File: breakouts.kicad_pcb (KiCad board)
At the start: 2 copper layers, 100 x 92.6 mm, 211 parts, among them IC901 ATTINY85-S, J1101 USB_MINI-B, J1201 JACK_5P, J201 USB_MINI-B, J301 USB_MINI-B, J401 SMA, J801 USB_MINI-B, K1201 CONN_3, K1301 CONN_3, K601 CONN_3, K801 CONN_3, P1001 CONN_4, P1002 CONN_4, P1101 CONN_6, P1102 CONN_6, P1201 CONN_2, P1202 CONN_2, P1203 CONN_2, P1301 CONN_2, P201 CONN_2, P202 CONN_2, P203 CONN_2, P301 CONN_6, P302 CONN_6, P401 CONN_8, P402 CONN_8, P501 CONN_2, P502 CONN_2, P701 POWER, P702 PORT B, P703 PORT C, P704 PORT D, P705 ISP, P801 PORT B, P802 PORT C, P803 PORT D, P804 ISP, P901 CONN_8, P902 ISP, SW701 SW_PUSH, SW801 SW_PUSH, SW901 SW_PUSH, U1001 SST25VF016B, U1101 FT230X-QFN, U1201 TDA1517ATW, U1301 MCP7940M, U301 FT230X, U401 MRF49XA, U501 SP6641A/B, U601 NX1117C33Z, U701 ATMEGA88PA-A, U801 ATMEGA32U2, X1301 32.768kHz, X401 10MHz, X701 12MHz 18pF, X801 16MHz 18pF

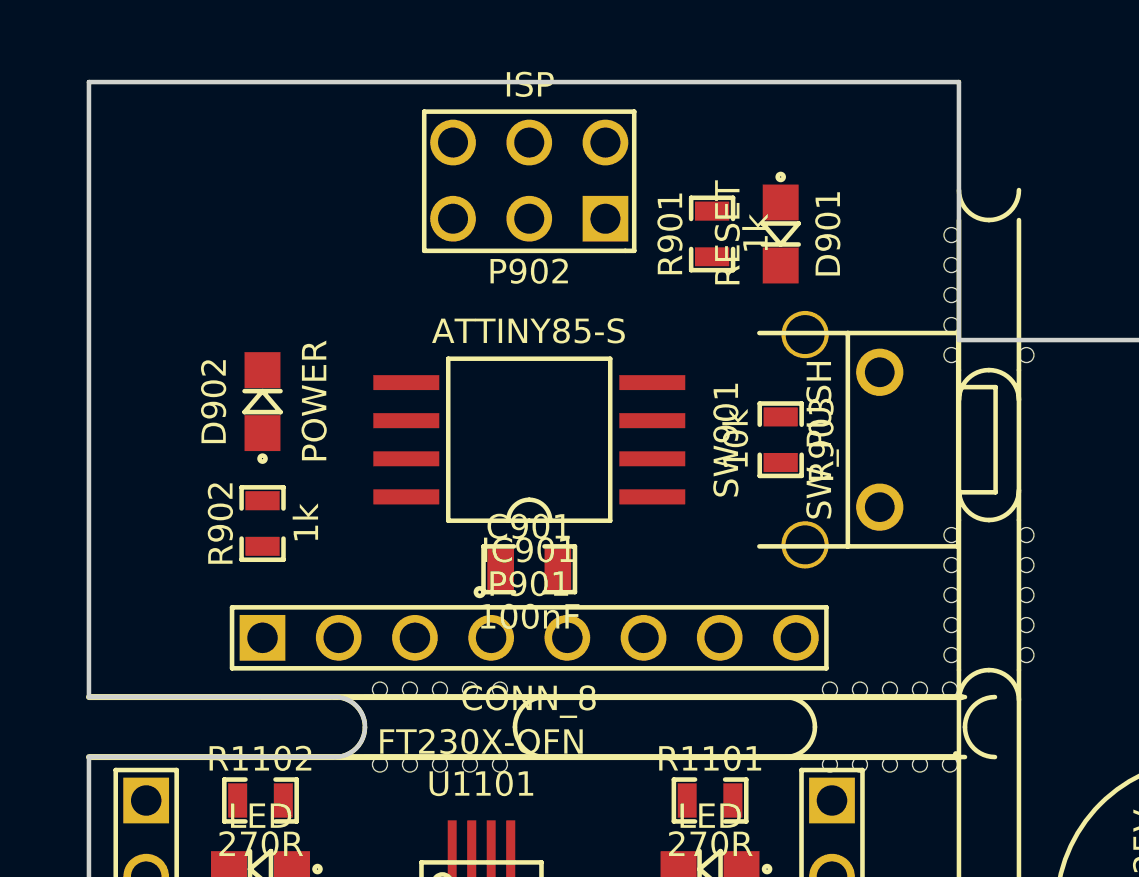
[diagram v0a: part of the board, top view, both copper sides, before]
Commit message: Route AVR ATtinyx5 board
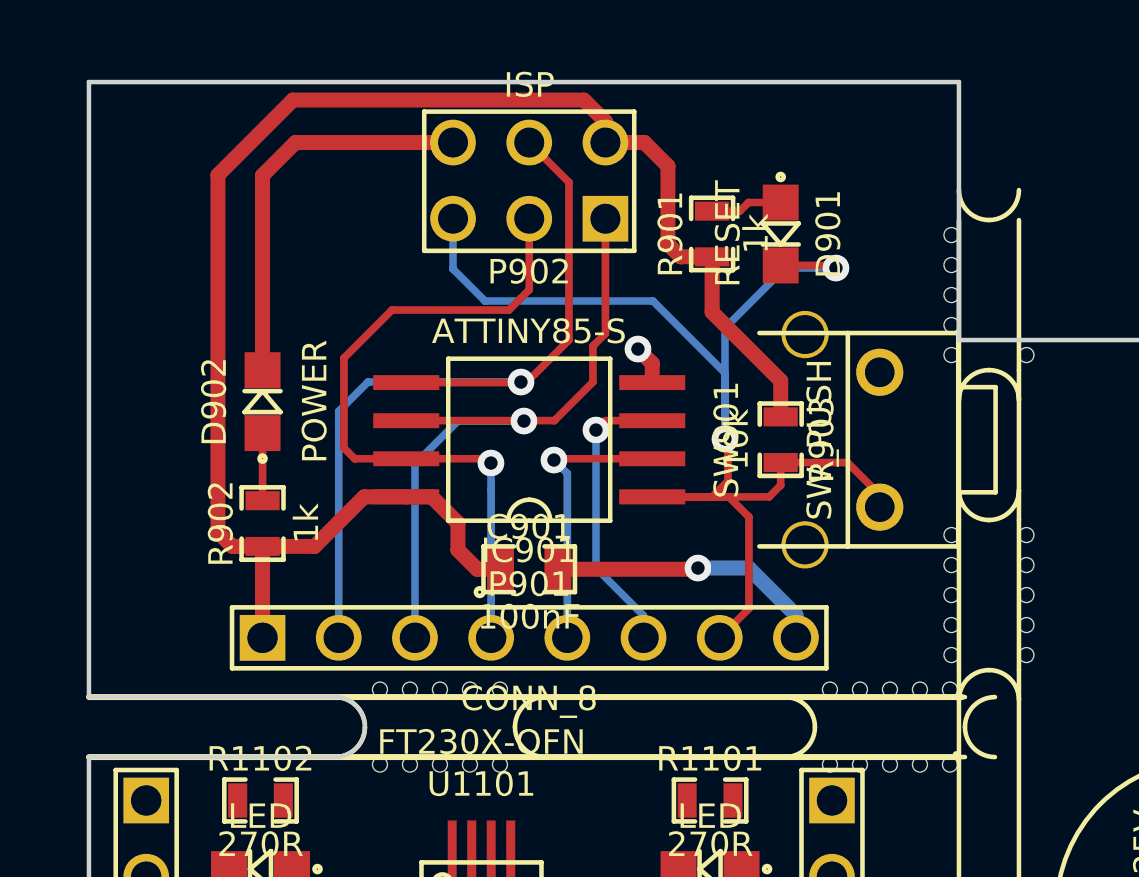
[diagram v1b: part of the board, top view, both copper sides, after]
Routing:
- net VCC8: track 0.00 -> 54.7 mm
- net /AVR-ATtinyx5/PB5: track 0.00 -> 44.0 mm, vias 0 -> 2
- net /AVR-ATtinyx5/MOSI: track 0.00 -> 27.2 mm, vias 0 -> 1
- net GND8: track 0.00 -> 24.0 mm, vias 0 -> 2
- net /AVR-ATtinyx5/PB2: track 0.00 -> 23.4 mm, vias 0 -> 1
- net /AVR-ATtinyx5/MISO: track 0.00 -> 22.4 mm, vias 0 -> 1
- net /AVR-ATtinyx5/PB4: track 0.00 -> 9.59 mm, vias 0 -> 1
- net /AVR-ATtinyx5/PB3: track 0.00 -> 9.40 mm, vias 0 -> 1
- net N-00000124: track 0.00 -> 2.40 mm
- net N-00000123: track 0.00 -> 2.25 mm
- added copper zone on B.Cu, net GND8

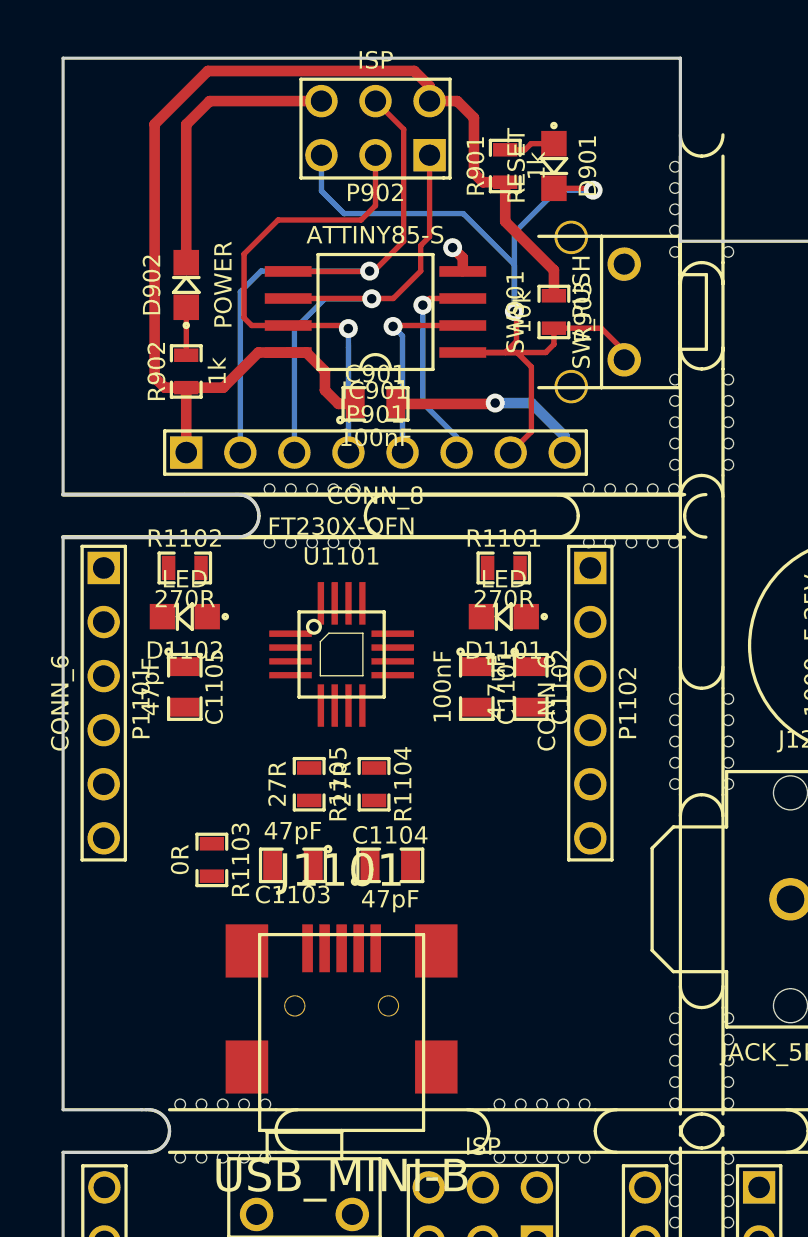
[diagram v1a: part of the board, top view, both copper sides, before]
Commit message: Rework and route FT230X-QFN board
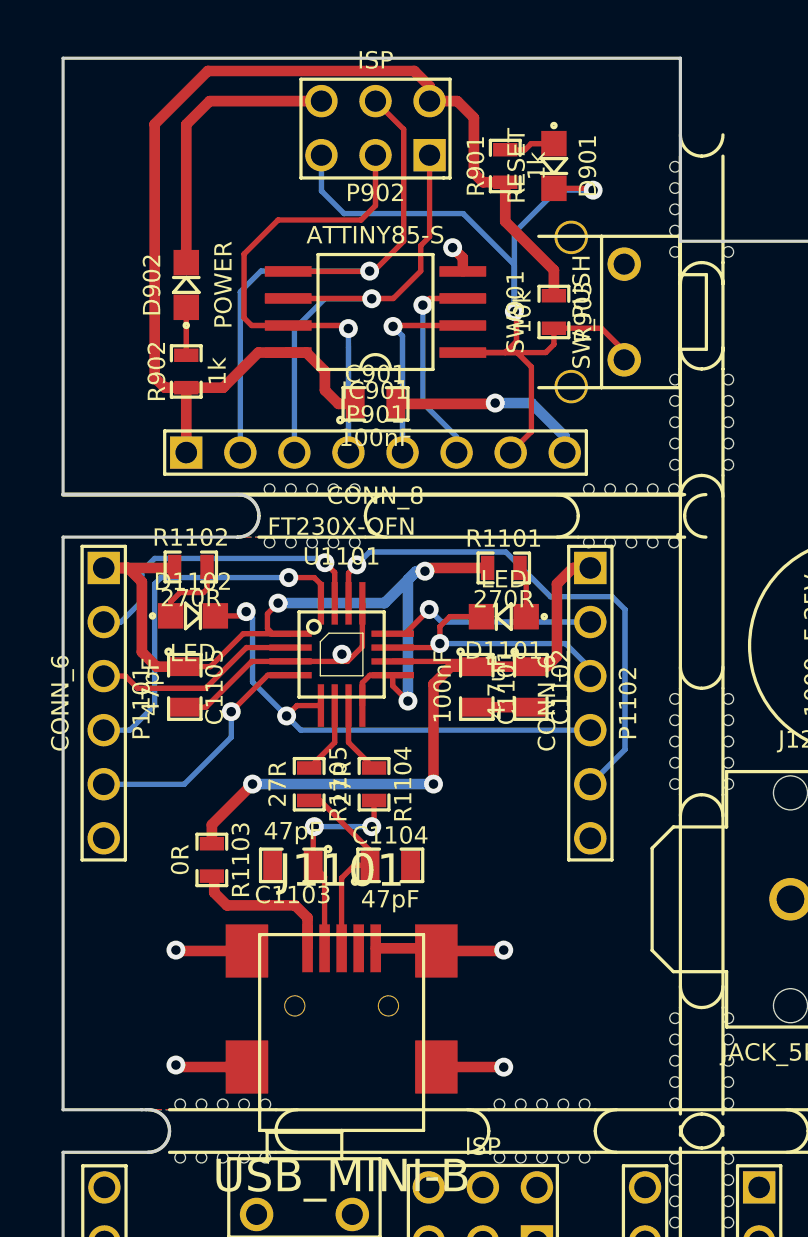
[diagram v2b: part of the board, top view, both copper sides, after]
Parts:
- moved D1102 0.38 mm to (32.1, 81.1), turned to 0 degrees
- moved R1102 0.29 mm to (32.0, 78.8)
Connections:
- J1101 pad 4: N-00000154 -> (no net)
- J1201 pad 3: N-00000177 -> (no net)
- J1201 pad 4: N-00000178 -> (no net)
- J201 pad 4: N-000007 (its old number) -> (no net)
- J301 pad 4: N-0000025 -> (no net)
- J801 pad 4: N-0000092 (its old number) -> (no net)
- P1101 pad 1: VCC3 -> /FT230X-QFN/VCCIO
- P1102 pad 1: /FT230X-QFN/VCCIO -> VCC3
- U1201 pad 1: N-00000170 (its old number) -> (no net)
- U1201 pad 14: N-00000176 -> (no net)
- U1201 pad 19: N-00000166 (its old number) -> (no net)
- U1201 pad 2: N-00000171 -> (no net)
- U1201 pad 20: N-00000175 -> (no net)
- U1201 pad 6: N-00000172 -> (no net)
- U1201 pad 7: N-00000173 -> (no net)
- U1301 pad 3: N-00000183 (its old number) -> (no net)
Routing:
- net /FT230X-QFN/VCCIO: track 0.00 -> 40.2 mm, vias 0 -> 3
- net VCC3: track 0.00 -> 32.5 mm, vias 0 -> 2
- net GND3: track 0.00 -> 30.2 mm, vias 0 -> 5
- net /FT230X-QFN/CBUS3: track 0.00 -> 24.8 mm, vias 0 -> 1
- net /FT230X-QFN/CBUS2: track 0.00 -> 23.6 mm, vias 0 -> 2
- net /FT230X-QFN/~RTS: track 0.00 -> 17.5 mm, vias 0 -> 1
- net /FT230X-QFN/TxD: track 0.00 -> 14.6 mm, vias 0 -> 1
- net /FT230X-QFN/CBUS1: track 0.00 -> 13.2 mm, vias 0 -> 1
- net /FT230X-QFN/~CTS: track 0.00 -> 11.6 mm, vias 0 -> 1
- net /FT230X-QFN/CBUS0: track 0.00 -> 10.00 mm, vias 0 -> 1
- net N-00000151: track 0.00 -> 9.93 mm, vias 0 -> 2
- net /FT230X-QFN/RxD: track 0.00 -> 9.81 mm
- net N-00000152: track 0.00 -> 9.41 mm
- net N-00000150: track 0.00 -> 7.13 mm
- net N-00000156: track 0.00 -> 3.65 mm
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- added copper zone on B.Cu, net GND3
- added copper zone on F.Cu, net GND3
- added copper zone on F.Cu, net GND8

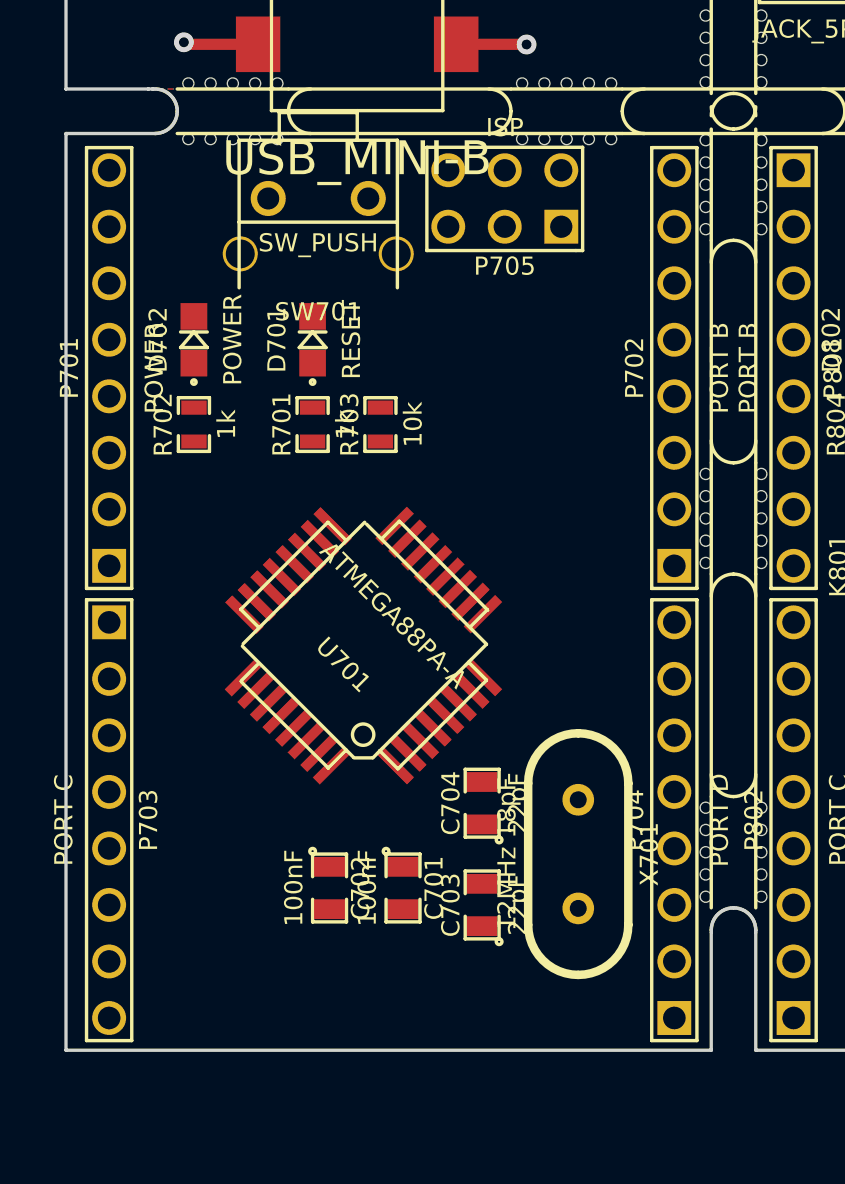
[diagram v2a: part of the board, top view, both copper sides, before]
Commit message: Route ATmegax8 board
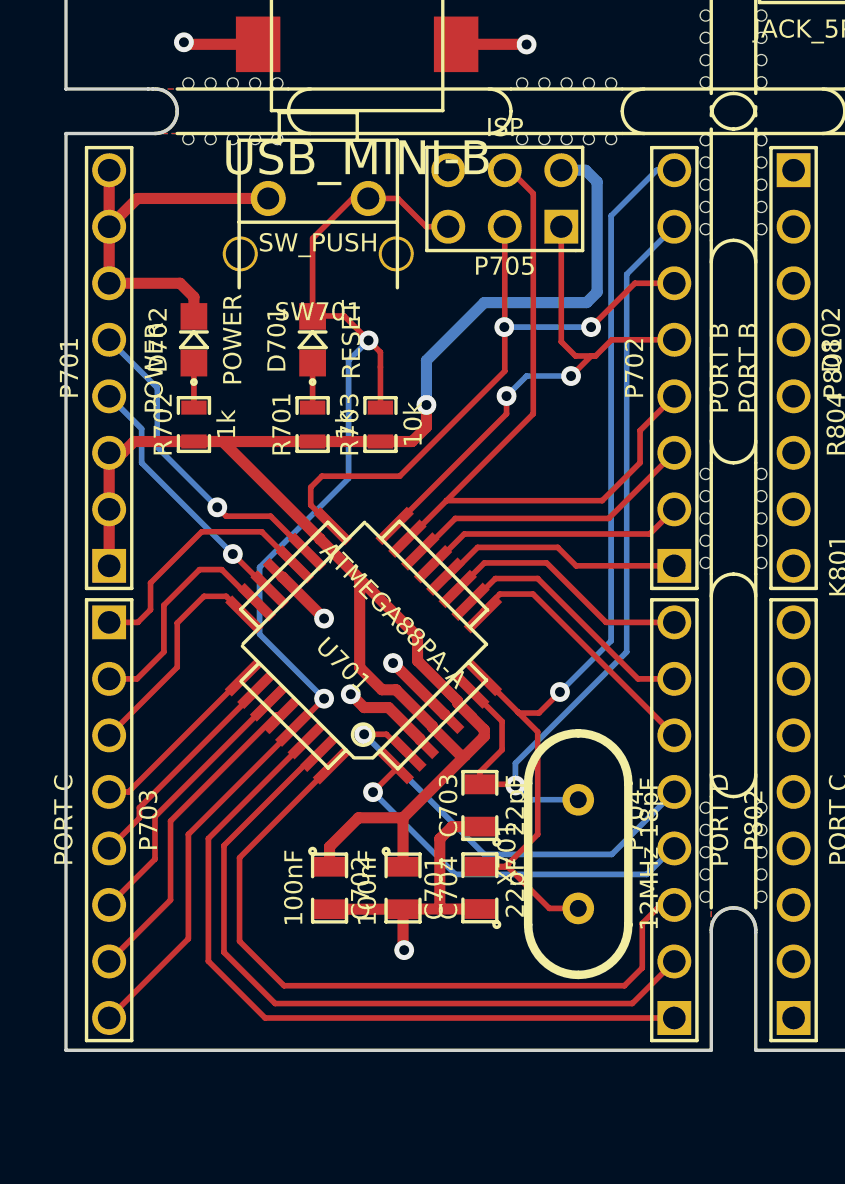
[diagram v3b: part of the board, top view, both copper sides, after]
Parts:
- moved C703 4.47 mm to (44.6, 136.5)
- moved C704 3.80 mm to (44.6, 140.2)
- turned X701 to 90 degrees
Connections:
- P701 pad 4: /AVR-ATmegax8/ADC6 -> /AVR-ATmegax8/ADC7
- P701 pad 5: /AVR-ATmegax8/ADC7 -> /AVR-ATmegax8/ADC6
- P703 pad 1: /AVR-ATmegax8/PC0 -> /AVR-ATmegax8/AREF
- P703 pad 2: /AVR-ATmegax8/PC1 -> /AVR-ATmegax8/PC0
- P703 pad 3: /AVR-ATmegax8/PC2 -> /AVR-ATmegax8/PC1
- P703 pad 4: /AVR-ATmegax8/PC3 -> /AVR-ATmegax8/PC2
- P703 pad 5: /AVR-ATmegax8/PC4 -> /AVR-ATmegax8/PC3
- P703 pad 6: /AVR-ATmegax8/PC5 -> /AVR-ATmegax8/PC4
- P703 pad 7: /AVR-ATmegax8/PC6 -> /AVR-ATmegax8/PC5
- P703 pad 8: /AVR-ATmegax8/AREF -> /AVR-ATmegax8/PC6
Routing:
- net VCC6: track 0.00 -> 80.5 mm, vias 0 -> 1
- net /AVR-ATmegax8/PC6: track 0.00 -> 54.8 mm, vias 0 -> 2
- net /AVR-ATmegax8/PB7: track 0.00 -> 44.9 mm, vias 0 -> 1
- net GND6: track 0.00 -> 41.5 mm, vias 0 -> 4
- net /AVR-ATmegax8/PB6: track 0.00 -> 38.0 mm, vias 0 -> 1
- net /AVR-ATmegax8/PD0: track 0.00 -> 33.8 mm
- net /AVR-ATmegax8/PD1: track 0.00 -> 32.8 mm
- net /AVR-ATmegax8/PD2: track 0.00 -> 32.7 mm
- net /AVR-ATmegax8/MOSI: track 0.00 -> 32.6 mm
- net /AVR-ATmegax8/PB5: track 0.00 -> 28.1 mm, vias 0 -> 2
- net /AVR-ATmegax8/MISO: track 0.00 -> 23.5 mm, vias 0 -> 2
- net /AVR-ATmegax8/PD4: track 0.00 -> 19.6 mm, vias 0 -> 1
- net /AVR-ATmegax8/PD3: track 0.00 -> 17.2 mm, vias 0 -> 1
- net /AVR-ATmegax8/PC5: track 0.00 -> 14.4 mm
- net /AVR-ATmegax8/ADC6: track 0.00 -> 14.4 mm, vias 0 -> 1
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- added copper zone on B.Cu, net GND6
- added copper zone on F.Cu, net GND6

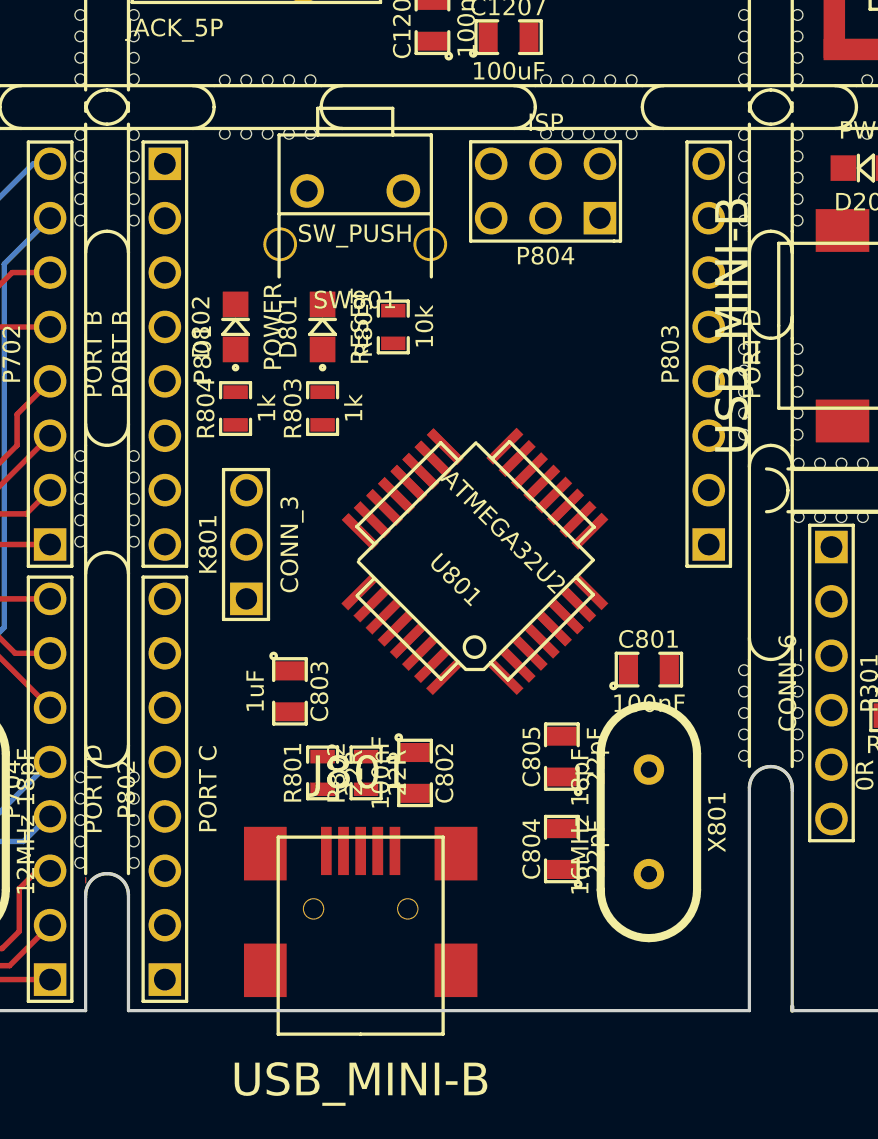
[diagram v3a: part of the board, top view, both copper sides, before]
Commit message: Route ATmegaxU2 board
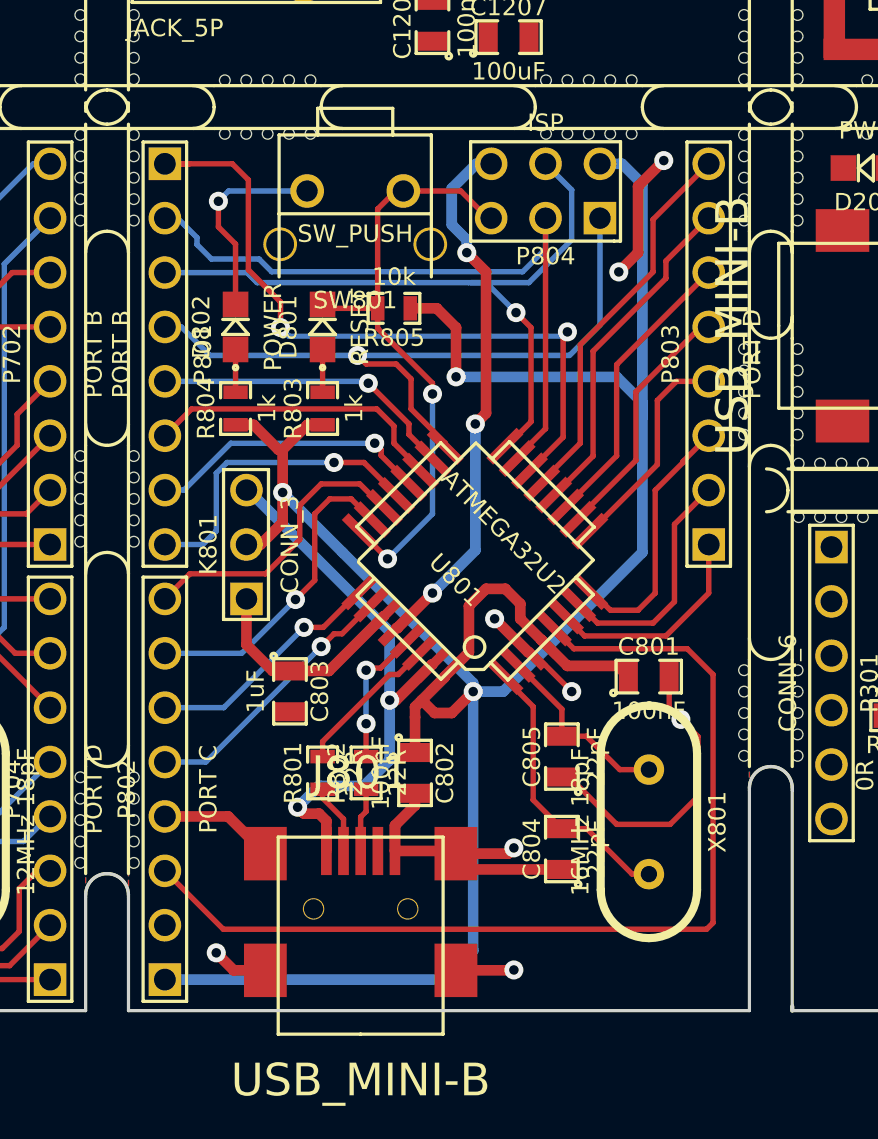
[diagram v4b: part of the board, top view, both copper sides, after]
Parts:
- moved R805 0.87 mm to (69.4, 114.7), turned to 180 degrees
- moved C801 0.33 mm to (81.3, 131.9)
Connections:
- P802 pad 1: VCC7 -> /AVR-ATmegaxU2/AVR_VCC
- P804 pad 2: VCC7 -> /AVR-ATmegaxU2/AVR_VCC
- R803 pad 1: VCC7 -> /AVR-ATmegaxU2/AVR_VCC
- R804 pad 1: VCC7 -> /AVR-ATmegaxU2/AVR_VCC
- R805 pad 1: VCC7 -> /AVR-ATmegaxU2/AVR_VCC
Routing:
- net /AVR-ATmegaxU2/AVR_VCC: track 0.00 -> 116.3 mm, vias 0 -> 3
- net GND7: track 0.00 -> 78.6 mm, vias 0 -> 10
- net /AVR-ATmegaxU2/PC2: track 0.00 -> 46.8 mm
- net /AVR-ATmegaxU2/MOSI: track 0.00 -> 33.8 mm, vias 0 -> 1
- net /AVR-ATmegaxU2/PB0: track 0.00 -> 33.8 mm, vias 0 -> 2
- net /AVR-ATmegaxU2/MISO: track 0.00 -> 33.2 mm, vias 0 -> 1
- net /AVR-ATmegaxU2/PB1: track 0.00 -> 32.7 mm
- net /AVR-ATmegaxU2/~RESET: track 0.00 -> 28.9 mm, vias 0 -> 2
- net N-0000095: track 0.00 -> 26.3 mm, vias 0 -> 2
- net /AVR-ATmegaxU2/PD7: track 0.00 -> 18.1 mm
- net /AVR-ATmegaxU2/PD6: track 0.00 -> 15.9 mm
- net /AVR-ATmegaxU2/PC6: track 0.00 -> 14.9 mm, vias 0 -> 1
- net /AVR-ATmegaxU2/PB7: track 0.00 -> 14.6 mm, vias 0 -> 1
- net /AVR-ATmegaxU2/PB4: track 0.00 -> 14.3 mm, vias 0 -> 1
- net /AVR-ATmegaxU2/PB5: track 0.00 -> 14.2 mm
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- added copper zone on B.Cu, net GND7
- added copper zone on F.Cu, net GND7
